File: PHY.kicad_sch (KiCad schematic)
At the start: 50 parts, among them U1 LAN83C185-JT, Y1 25 MHz

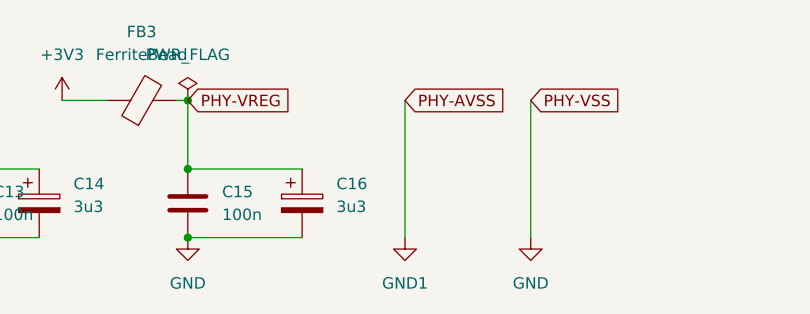
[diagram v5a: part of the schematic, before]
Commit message: moved some resitors around to make myself feel better
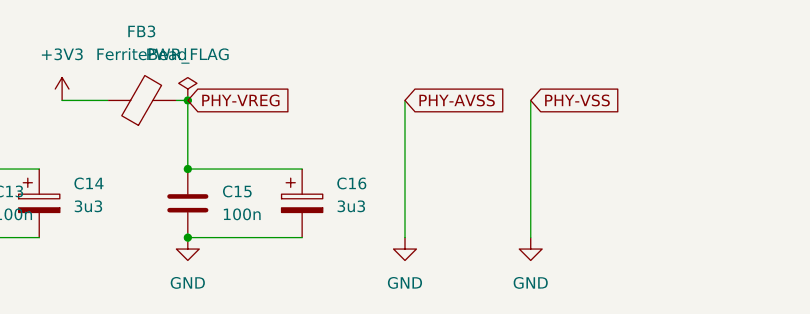
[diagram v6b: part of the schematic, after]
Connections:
- net GND1 is gone; now on net GND: U1.49 (AVSS1), U1.52 (AVSS2), U1.58 (AVSS3), U1.60 (AVSS4), U1.62 (AVSS5)
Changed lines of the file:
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@@
     (pin "2")
+  )
+  (symbol (lib_id "power:GND") (at 144.78 187.96 0) (unit 1)
+    (in_bom yes) (on_board yes) (fields_autoplaced)
+    (property "Reference" "#PWR0110" (id 0) (at 144.78 194.31 0)
+      (effects (font (size 1.27 1.27)) hide)
+    )
+    (property "Value" "GND" (id 1) (at 144.78 193.04 0))
+    (property "Footprint" "" (id 2) (at 144.78 187.96 0)
+      (effects (font (size 1.27 1.27)) hide)
+    )
+    (property "Datasheet" "" (id 3) (at 144.78 187.96 0)
+      (effects (font (size 1.27 1.27)) hide)
+    )
+    (pin "1")
   )
   (symbol (lib_id "power:+3V3") (at 106.68 172.72 0) (unit 1)
@@
     (pin "2")
   )
-  (symbol (lib_id "power:GND1") (at 144.78 187.96 0) (unit 1)
-    (in_bom yes) (on_board yes) (fields_autoplaced)
-    (property "Reference" "#PWR0110" (id 0) (at 144.78 194.31 0)
-      (effects (font (size 1.27 1.27)) hide)
-    )
-    (property "Value" "GND1" (id 1) (at 144.78 193.04 0))
-    (property "Footprint" "" (id 2) (at 144.78 187.96 0)
-      (effects (font (size 1.27 1.27)) hide)
-    )
-    (property "Datasheet" "" (id 3) (at 144.78 187.96 0)
-      (effects (font (size 1.27 1.27)) hide)
-    )
-    (pin "1")
-  )
   (symbol (lib_id "Device:R") (at 210.82 129.54 180) (unit 1)

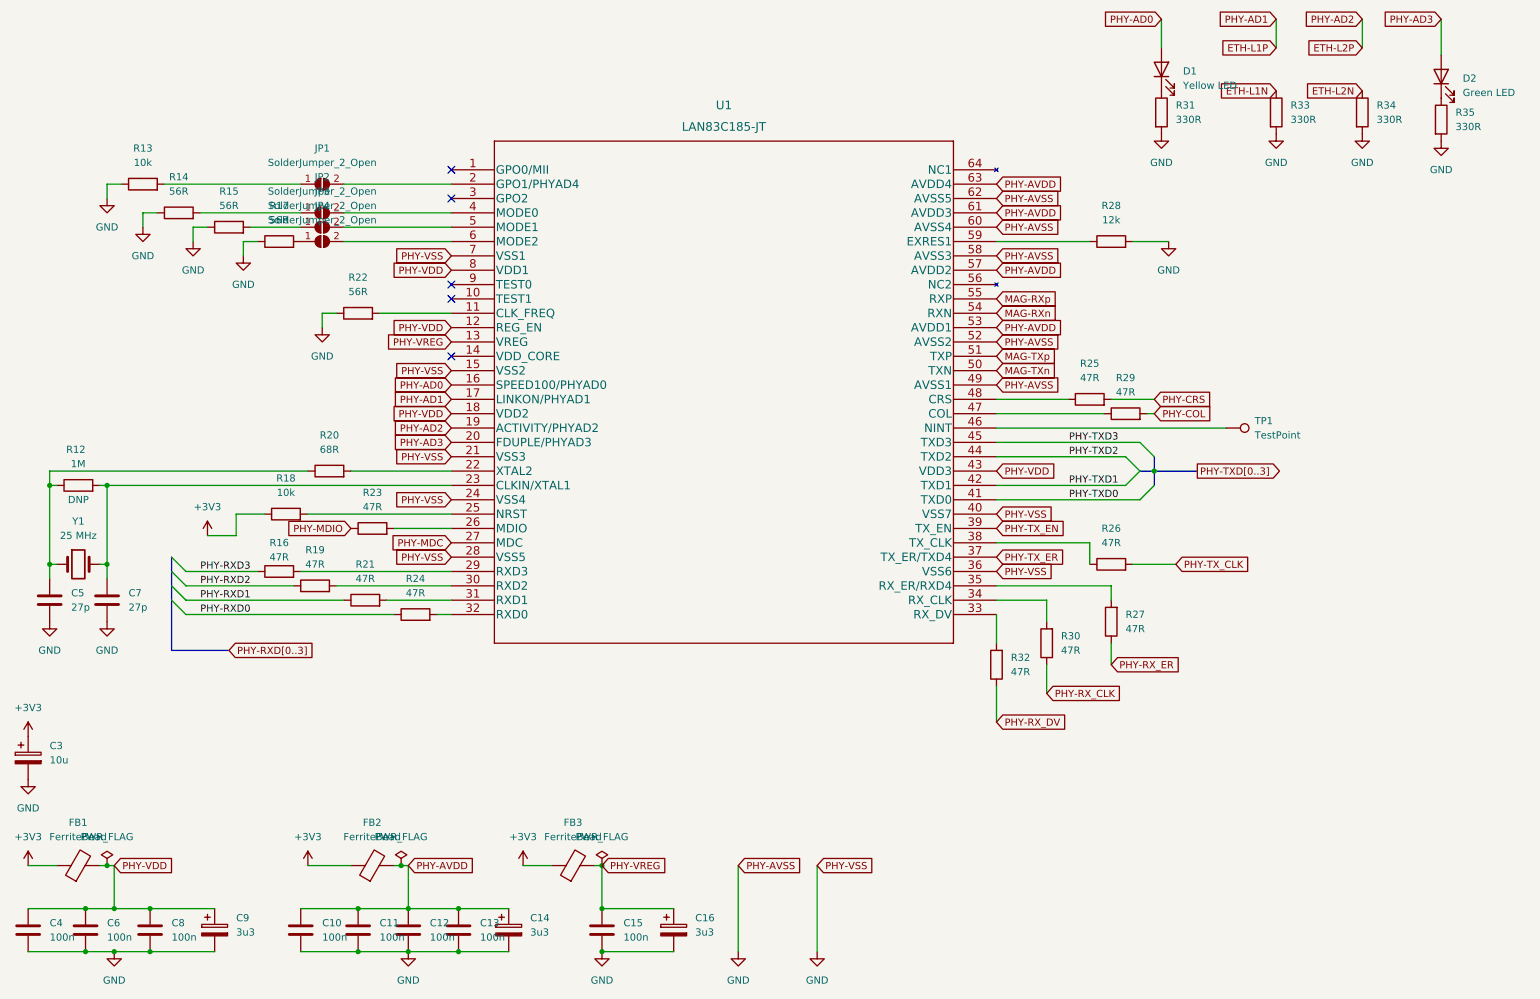
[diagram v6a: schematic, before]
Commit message: Place and route optic side parts
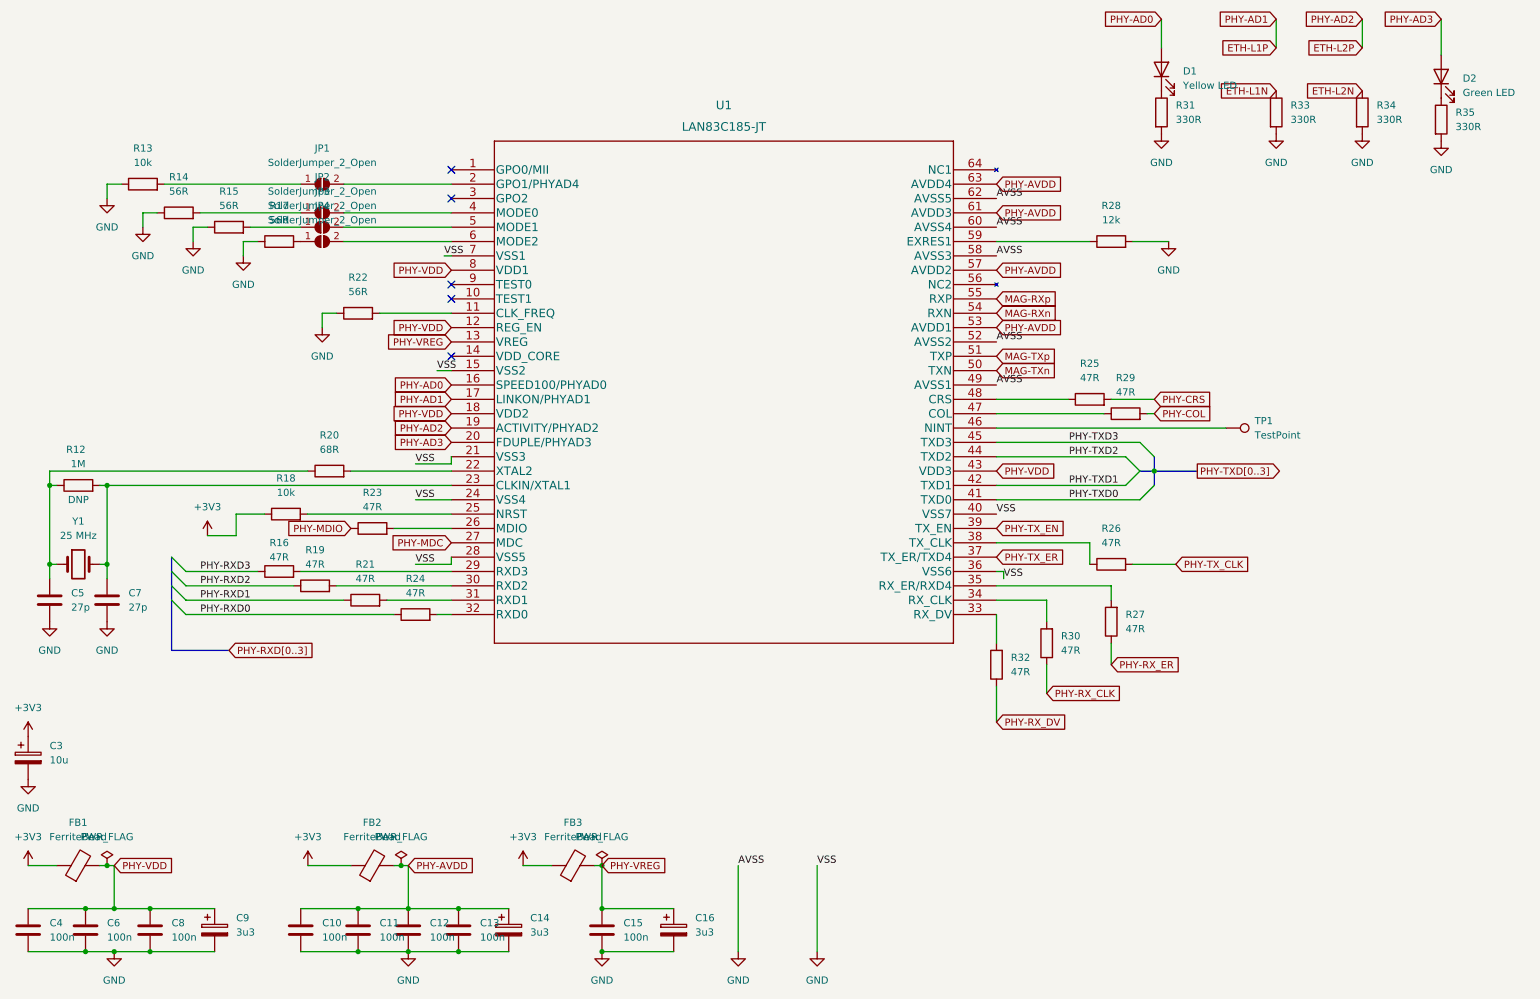
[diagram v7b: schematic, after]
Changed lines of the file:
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@@
+    (stroke (width 0) (type default) (color 0 0 0 0))
+  )
+  (wire (pts (xy 87.63 101.6) (xy 93.98 101.6))
+    (stroke (width 0) (type default) (color 0 0 0 0))
+  )
+  (wire (pts (xy 191.77 120.65) (xy 190.5 120.65))
     (stroke (width 0) (type default) (color 0 0 0 0))
   )
@@
     (stroke (width 0) (type default) (color 0 0 0 0))
   )
+  (wire (pts (xy 93.98 119.38) (xy 93.98 118.11))
+    (stroke (width 0) (type default) (color 0 0 0 0))
+  )
   (wire (pts (xy 71.12 74.93) (xy 71.12 77.47))
     (stroke (width 0) (type default) (color 0 0 0 0))
@@
     (stroke (width 0) (type default) (color 0 0 0 0))
   )
+  (wire (pts (xy 91.44 85.09) (xy 93.98 85.09))
+    (stroke (width 0) (type default) (color 0 0 0 0))
+  )
   (wire (pts (xy 33.02 105.41) (xy 33.02 119.38))
     (stroke (width 0) (type default) (color 0 0 0 0))
@@
     (stroke (width 0) (type default) (color 0 0 0 0))
   )
+  (wire (pts (xy 92.71 64.77) (xy 93.98 64.77))
+    (stroke (width 0) (type default) (color 0 0 0 0))
+  )
   (wire (pts (xy 86.36 172.72) (xy 86.36 180.34))
     (stroke (width 0) (type default) (color 0 0 0 0))
@@
     (stroke (width 0) (type default) (color 0 0 0 0))
   )
+  (wire (pts (xy 87.63 119.38) (xy 93.98 119.38))
+    (stroke (width 0) (type default) (color 0 0 0 0))
+  )
   (wire (pts (xy 46.99 125.73) (xy 74.93 125.73))
     (stroke (width 0) (type default) (color 0 0 0 0))
@@
     (stroke (width 0) (type default) (color 0 0 0 0))
   )
+  (wire (pts (xy 191.77 121.92) (xy 191.77 120.65))
+    (stroke (width 0) (type default) (color 0 0 0 0))
+  )
   (wire (pts (xy 199.39 125.73) (xy 199.39 129.54))
     (stroke (width 0) (type default) (color 0 0 0 0))
   )
+  (wire (pts (xy 93.98 101.6) (xy 93.98 100.33))
+    (stroke (width 0) (type default) (color 0 0 0 0))
+  )
   (wire (pts (xy 207.01 115.57) (xy 207.01 119.38))
     (stroke (width 0) (type default) (color 0 0 0 0))
   )
+  (wire (pts (xy 87.63 107.95) (xy 93.98 107.95))
+    (stroke (width 0) (type default) (color 0 0 0 0))
+  )
   (wire (pts (xy 190.5 140.97) (xy 190.5 147.32))
     (stroke (width 0) (type default) (color 0 0 0 0))
@@
     (stroke (width 0) (type default) (color 0 0 0 0))
   )
+  (label "VSS" (at 87.63 101.6 0)
+    (effects (font (size 1.27 1.27)) (justify left bottom))
+  )
   (label "PHY-RXD0" (at 58.42 128.27 180)
     (effects (font (size 1.27 1.27)) (justify right bottom))
   )
+  (label "VSS" (at 191.77 121.92 0)
+    (effects (font (size 1.27 1.27)) (justify left bottom))
+  )
   (label "PHY-RXD1" (at 58.42 125.73 180)
     (effects (font (size 1.27 1.27)) (justify right bottom))
   )
+  (label "VSS" (at 158.75 172.72 0)
+    (effects (font (size 1.27 1.27)) (justify left bottom))
+  )
+  (label "VSS" (at 92.71 64.77 0)
+    (effects (font (size 1.27 1.27)) (justify left bottom))
+  )
+  (label "AVSS" (at 190.5 80.01 0)
+    (effects (font (size 1.27 1.27)) (justify left bottom))
+  )
+  (label "VSS" (at 87.63 107.95 0)
+    (effects (font (size 1.27 1.27)) (justify left bottom))
+  )
   (label "PHY-RXD2" (at 58.42 123.19 180)
     (effects (font (size 1.27 1.27)) (justify right bottom))
   )
+  (label "VSS" (at 87.63 119.38 0)
+    (effects (font (size 1.27 1.27)) (justify left bottom))
+  )
   (label "PHY-TXD0" (at 212.09 107.95 180)
     (effects (font (size 1.27 1.27)) (justify right bottom))
@@
     (effects (font (size 1.27 1.27)) (justify right bottom))
   )
+  (label "VSS" (at 190.5 110.49 0)
+    (effects (font (size 1.27 1.27)) (justify left bottom))
+  )
+  (label "AVSS" (at 190.5 59.69 0)
+    (effects (font (size 1.27 1.27)) (justify left bottom))
+  )
+  (label "AVSS" (at 190.5 64.77 0)
+    (effects (font (size 1.27 1.27)) (justify left bottom))
+  )
+  (label "AVSS" (at 190.5 87.63 0)
+    (effects (font (size 1.27 1.27)) (justify left bottom))
+  )
+  (label "VSS" (at 91.44 85.09 0)
+    (effects (font (size 1.27 1.27)) (justify left bottom))
+  )
+  (label "AVSS" (at 144.78 172.72 0)
+    (effects (font (size 1.27 1.27)) (justify left bottom))
+  )
+  (label "AVSS" (at 190.5 54.61 0)
+    (effects (font (size 1.27 1.27)) (justify left bottom))
+  )
   (label "PHY-TXD2" (at 212.09 100.33 180)
     (effects (font (size 1.27 1.27)) (justify right bottom))
@@
     )
   )
-  (global_label "PHY-VSS" (shape input) (at 93.98 107.95 180) (fields_autoplaced)
-    (effects (font (size 1.27 1.27)) (justify right))
-    (property "Intersheet References" "${INTERSHEET_REFS}" (id 0) (at 82.7979 108.0294 0)
-      (effects (font (size 1.27 1.27)) (justify right) hide)
-    )
-  )
   (global_label "PHY-RX_DV" (shape input) (at 190.5 147.32 0) (fields_autoplaced)
     (effects (font (size 1.27 1.27)) (justify left))
@@
     )
   )
-  (global_label "PHY-AVSS" (shape input) (at 190.5 54.61 0) (fields_autoplaced)
-    (effects (font (size 1.27 1.27)) (justify left))
-    (property "Intersheet References" "${INTERSHEET_REFS}" (id 0) (at 202.7707 54.5306 0)
-      (effects (font (size 1.27 1.27)) (justify left) hide)
-    )
-  )
   (global_label "PHY-RX_CLK" (shape input) (at 199.39 142.24 0) (fields_autoplaced)
     (effects (font (size 1.27 1.27)) (justify left))
@@
     )
   )
-  (global_label "PHY-VSS" (shape input) (at 158.75 172.72 0) (fields_autoplaced)
-    (effects (font (size 1.27 1.27)) (justify left))
-    (property "Intersheet References" "${INTERSHEET_REFS}" (id 0) (at 169.9321 172.6406 0)
-      (effects (font (size 1.27 1.27)) (justify left) hide)
-    )
-  )
   (global_label "MAG-TXp" (shape input) (at 190.5 82.55 0) (fields_autoplaced)
     (effects (font (size 1.27 1.27)) (justify left))
@@
     )
   )
-  (global_label "PHY-VSS" (shape input) (at 93.98 100.33 180) (fields_autoplaced)
-    (effects (font (size 1.27 1.27)) (justify right))
-    (property "Intersheet References" "${INTERSHEET_REFS}" (id 0) (at 82.7979 100.4094 0)
-      (effects (font (size 1.27 1.27)) (justify right) hide)
-    )
-  )
-  (global_label "PHY-AVSS" (shape input) (at 190.5 64.77 0) (fields_autoplaced)
-    (effects (font (size 1.27 1.27)) (justify left))
-    (property "Intersheet References" "${INTERSHEET_REFS}" (id 0) (at 202.7707 64.6906 0)
-      (effects (font (size 1.27 1.27)) (justify left) hide)
-    )
-  )
   (global_label "PHY-VDD" (shape input) (at 93.98 77.47 180) (fields_autoplaced)
     (effects (font (size 1.27 1.27)) (justify right))
@@
     )
   )
-  (global_label "PHY-VSS" (shape input) (at 93.98 85.09 180) (fields_autoplaced)
-    (effects (font (size 1.27 1.27)) (justify right))
-    (property "Intersheet References" "${INTERSHEET_REFS}" (id 0) (at 82.7979 85.1694 0)
-      (effects (font (size 1.27 1.27)) (justify right) hide)
-    )
-  )
   (global_label "MAG-TXn" (shape input) (at 190.5 85.09 0) (fields_autoplaced)
     (effects (font (size 1.27 1.27)) (justify left))
@@
     )
   )
-  (global_label "PHY-VSS" (shape input) (at 190.5 110.49 0) (fields_autoplaced)
-    (effects (font (size 1.27 1.27)) (justify left))
-    (property "Intersheet References" "${INTERSHEET_REFS}" (id 0) (at 201.6821 110.4106 0)
-      (effects (font (size 1.27 1.27)) (justify left) hide)
-    )
-  )
   (global_label "PHY-TX_CLK" (shape input) (at 222.25 119.38 0) (fields_autoplaced)
     (effects (font (size 1.27 1.27)) (justify left))
@@
     )
   )
-  (global_label "PHY-AVSS" (shape input) (at 190.5 59.69 0) (fields_autoplaced)
-    (effects (font (size 1.27 1.27)) (justify left))
-    (property "Intersheet References" "${INTERSHEET_REFS}" (id 0) (at 202.7707 59.6106 0)
-      (effects (font (size 1.27 1.27)) (justify left) hide)
-    )
-  )
-  (global_label "PHY-VSS" (shape input) (at 93.98 64.77 180) (fields_autoplaced)
-    (effects (font (size 1.27 1.27)) (justify right))
-    (property "Intersheet References" "${INTERSHEET_REFS}" (id 0) (at 82.7979 64.8494 0)
-      (effects (font (size 1.27 1.27)) (justify right) hide)
-    )
-  )
   (global_label "PHY-AD0" (shape input) (at 93.98 87.63 180) (fields_autoplaced)
     (effects (font (size 1.27 1.27)) (justify right))
@@
     )
   )
-  (global_label "PHY-VSS" (shape input) (at 190.5 120.65 0) (fields_autoplaced)
-    (effects (font (size 1.27 1.27)) (justify left))
-    (property "Intersheet References" "${INTERSHEET_REFS}" (id 0) (at 201.6821 120.5706 0)
-      (effects (font (size 1.27 1.27)) (justify left) hide)
-    )
-  )
-  (global_label "PHY-VSS" (shape input) (at 93.98 118.11 180) (fields_autoplaced)
-    (effects (font (size 1.27 1.27)) (justify right))
-    (property "Intersheet References" "${INTERSHEET_REFS}" (id 0) (at 82.7979 118.1894 0)
-      (effects (font (size 1.27 1.27)) (justify right) hide)
-    )
-  )
   (global_label "PHY-VDD" (shape input) (at 93.98 67.31 180) (fields_autoplaced)
     (effects (font (size 1.27 1.27)) (justify right))
@@
     )
   )
-  (global_label "PHY-AVSS" (shape input) (at 190.5 80.01 0) (fields_autoplaced)
-    (effects (font (size 1.27 1.27)) (justify left))
-    (property "Intersheet References" "${INTERSHEET_REFS}" (id 0) (at 202.7707 79.9306 0)
-      (effects (font (size 1.27 1.27)) (justify left) hide)
-    )
-  )
-  (global_label "PHY-AVSS" (shape input) (at 144.78 172.72 0) (fields_autoplaced)
-    (effects (font (size 1.27 1.27)) (justify left))
-    (property "Intersheet References" "${INTERSHEET_REFS}" (id 0) (at 157.0507 172.6406 0)
-      (effects (font (size 1.27 1.27)) (justify left) hide)
-    )
-  )
   (global_label "PHY-AVDD" (shape input) (at 190.5 67.31 0) (fields_autoplaced)
     (effects (font (size 1.27 1.27)) (justify left))
@@
       (effects (font (size 1.27 1.27)) (justify left) hide)
     )
-  )
-  (global_label "PHY-AVSS" (shape input) (at 190.5 87.63 0) (fields_autoplaced)
-    (effects (font (size 1.27 1.27)) (justify left))
-    (property "Intersheet References" "${INTERSHEET_REFS}" (id 0) (at 202.7707 87.5506 0)
-      (effects (font (size 1.27 1.27)) (justify left) hide)
-    )
